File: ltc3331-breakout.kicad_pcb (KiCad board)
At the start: 2 copper layers, 100 x 100 mm, 61 parts, among them IC1 LTC3331, J1 CONN_01X04, J10 CONN_01X02_FEMALE, J11 CONN_01X04, J12 CONN_01X03, J13 CONN_01X03, J14 CONN_01X03, J15 CONN_02X12, J16 CONN_02X08, J17 CONN_02X08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

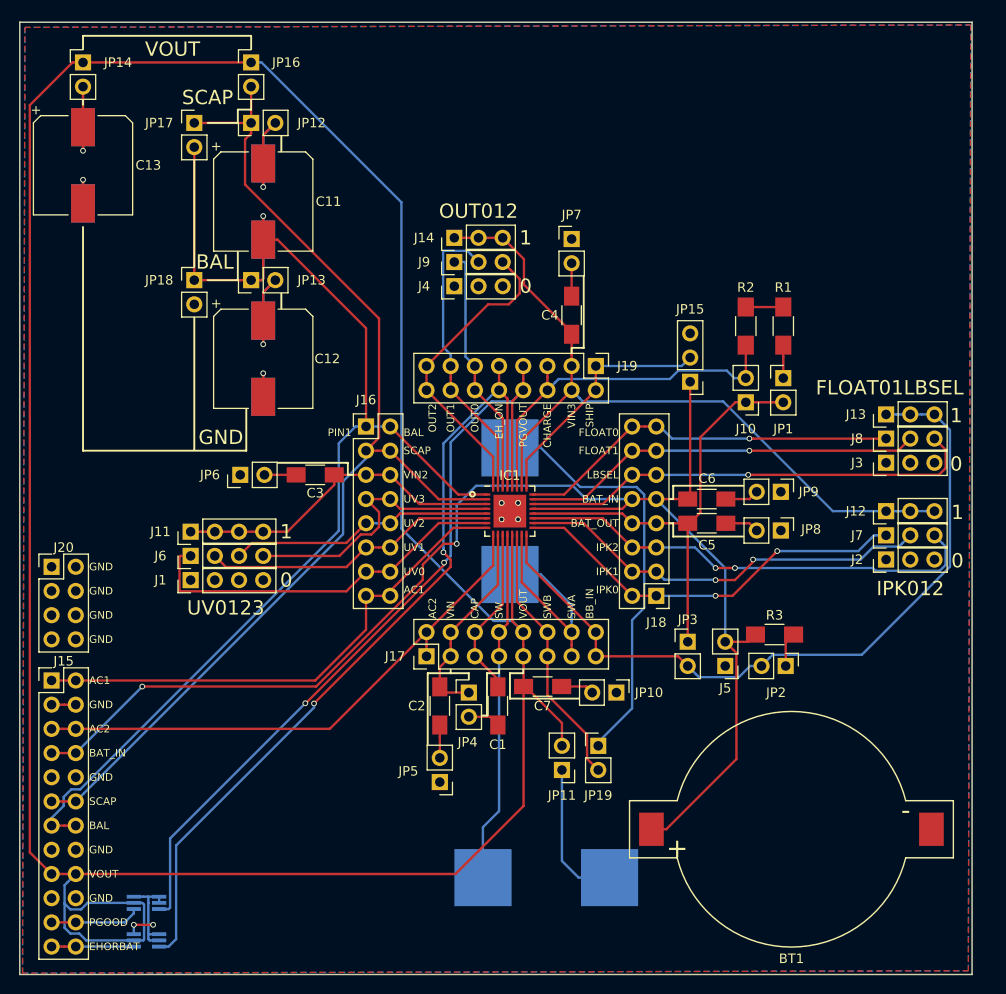
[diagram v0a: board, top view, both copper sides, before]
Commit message: routing cleanup, copper pour cleanup, added mounting holes and more silk screen labels
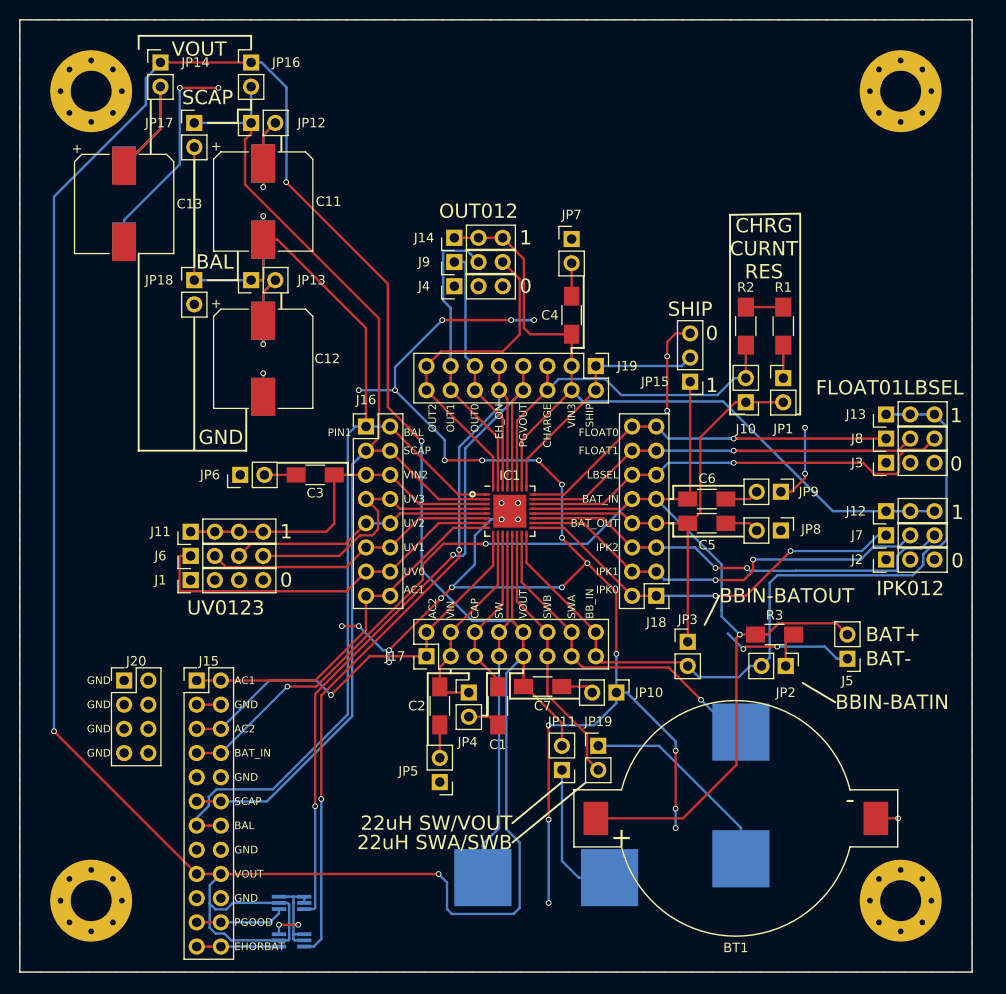
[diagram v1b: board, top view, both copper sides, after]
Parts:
- added REF**: MountingHole_4.3mm_M4_Pad_Via, Mounting_Holes:MountingHole_4.3mm_M4_Pad_Via, F.Cu at (142.5, 57.5)
- added REF**: MountingHole_4.3mm_M4_Pad_Via, Mounting_Holes:MountingHole_4.3mm_M4_Pad_Via, F.Cu at (142.5, 142.5)
- added REF**: MountingHole_4.3mm_M4_Pad_Via, Mounting_Holes:MountingHole_4.3mm_M4_Pad_Via, F.Cu at (57.5, 142.5)
- added REF**: MountingHole_4.3mm_M4_Pad_Via, Mounting_Holes:MountingHole_4.3mm_M4_Pad_Via, F.Cu at (57.5, 57.5)
- moved L2 38.5 mm to (125.7, 131.4), turned to 270 degrees
- moved U1 15.2 mm to (78.5, 142.7)
- moved U2 15.2 mm to (78.5, 146.7)
- moved J15 15.2 mm to (68.6, 119.4)
- moved J20 14.2 mm to (61.0, 119.4)
- moved J5 12.8 mm to (136.9, 117.1)
- moved JP14 8.13 mm to (64.8, 54.5)
- moved BT1 5.95 mm to (125.2, 133.9)
- moved C13 5.93 mm to (61.0, 69.3)
- moved C10 5.89 mm to (61.0, 69.3)
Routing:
- net GND: track 26.1 -> 237.9 mm, vias 8 -> 41
- net Net-(JP19-Pad1): track 44.5 -> 22.2 mm
- net /AC1: track 54.7 -> 39.5 mm
- net /AC2: track 59.3 -> 44.3 mm, vias 0 -> 1
- net Net-(C10-Pad1): track 9.21 -> 19.7 mm, vias 1 -> 0
- net /SWA: track 25.6 -> 36.1 mm, vias 0 -> 1
- net /EH_ON: track 87.8 -> 80.7 mm
- net /PGVOUT: track 85.5 -> 78.7 mm
- net /BAT_IN: track 151.9 -> 148.0 mm, vias 2 -> 3
- net /SCAP: track 117.7 -> 114.2 mm
- net /BAL: track 136.5 -> 133.1 mm
- net /BB_IN: track 80.5 -> 83.6 mm
- net /IPK2: track 49.5 -> 46.9 mm
- net /VIN3: track 79.9 -> 82.5 mm
- net /OUT2: track 32.7 -> 35.2 mm
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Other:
- net class SmallSignal removed
- board text added: "22uH SW/VOUT"
- board text added: "22uH SWA/SWB"
- board text added: "BAT+"
- board text added: "BAT-"
- board text added: "BBIN-BATIN"
- board text added: "BBIN-BATOUT"
- board text added: "CHRG CURNT RES"

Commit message: fixed silkscreen bug, layout cleanup, production stuff
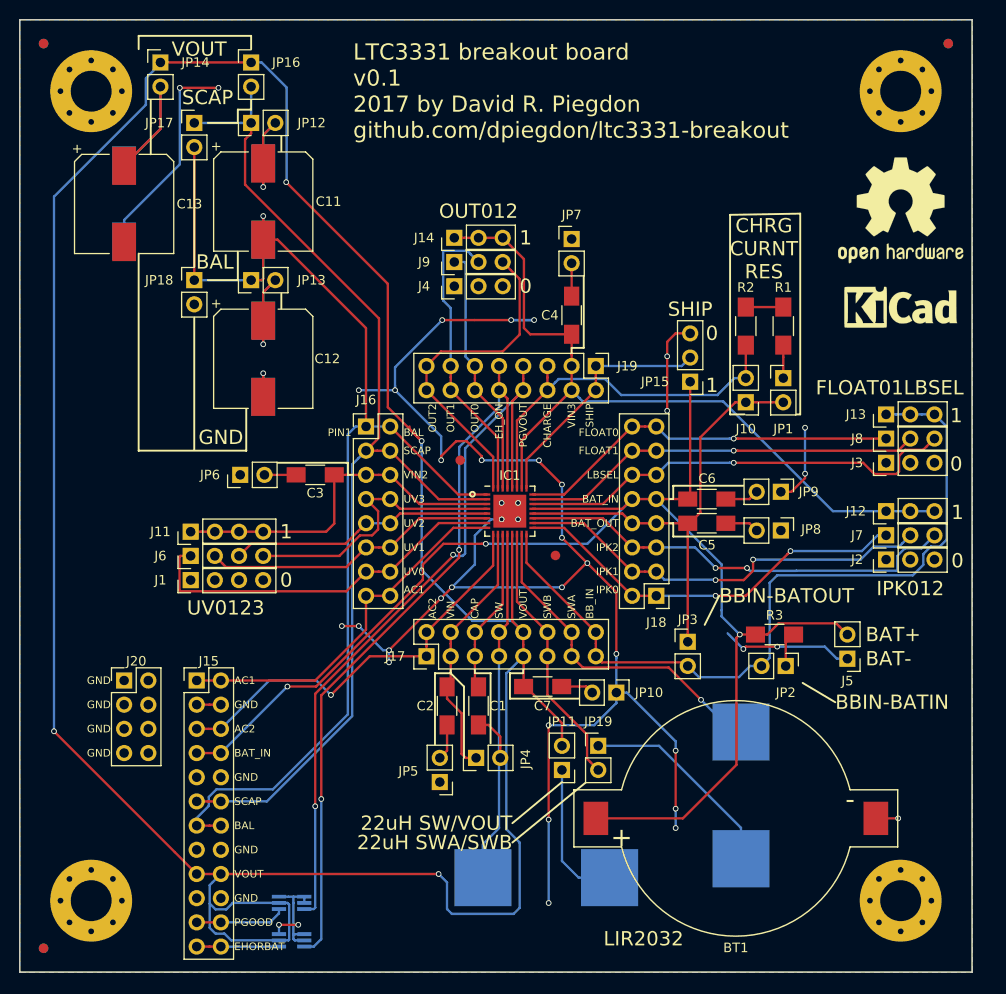
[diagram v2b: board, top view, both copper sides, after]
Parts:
- added FID**: fiducial_i.5mm_o1.5mm, footprints:fiducial_i.5mm_o1.5mm, B.Cu at (147.5, 52.5)
- added FID**: fiducial_i.5mm_o1.5mm, footprints:fiducial_i.5mm_o1.5mm, B.Cu at (52.5, 147.5)
- added FID**: fiducial_i.5mm_o1.5mm, footprints:fiducial_i.5mm_o1.5mm, B.Cu at (52.5, 52.5)
- added FID**: fiducial_i.5mm_o1.5mm, footprints:fiducial_i.5mm_o1.5mm, F.Cu at (106.2, 106.2)
- added FID**: fiducial_i.5mm_o1.5mm, footprints:fiducial_i.5mm_o1.5mm, F.Cu at (96.2, 96.2)
- added FID**: fiducial_i.5mm_o1.5mm, footprints:fiducial_i.5mm_o1.5mm, F.Cu at (52.5, 147.5)
- added FID**: fiducial_i.5mm_o1.5mm, footprints:fiducial_i.5mm_o1.5mm, F.Cu at (147.5, 52.5)
- added FID**: fiducial_i.5mm_o1.5mm, footprints:fiducial_i.5mm_o1.5mm, F.Cu at (52.5, 52.5)
- added REF**: KiCAD Logo, Symbols:Symbol_KiCAD-Logo_CopperAndSilkScreenTop, F.Cu at (142.5, 80.0)
- added REF***: OSHW-Logo2_14.6x12mm_SilkScreen, Symbols:OSHW-Logo2_14.6x12mm_SilkScreen, F.Cu at (142.5, 70.0)
- moved JP4 6.90 mm to (97.9, 127.5), turned to 90 degrees
- moved C1 2.03 mm to (98.2, 122.0)
- moved C2 0.76 mm to (94.9, 122.0)
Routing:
- net /VIN: track 21.9 -> 27.6 mm
- net GND: track 237.9 -> 240.3 mm
- net Net-(C1-Pad2): track 3.40 -> 5.02 mm
- net /CAP: track 18.3 -> 17.4 mm
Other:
- board text added: "LIR2032"
- board text added: "LTC3331 breakout board v0.1 2017 by David R. Piegdon github.com/dpiegdon/ltc3331-breakout"
